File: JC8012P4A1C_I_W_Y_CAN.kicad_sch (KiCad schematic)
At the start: 31 parts, among them J1 610110249121, J2 68711414522, J3 653104131822, Q1 DMP6050SSD, U1 TLE9250VSJ, U2 171030601

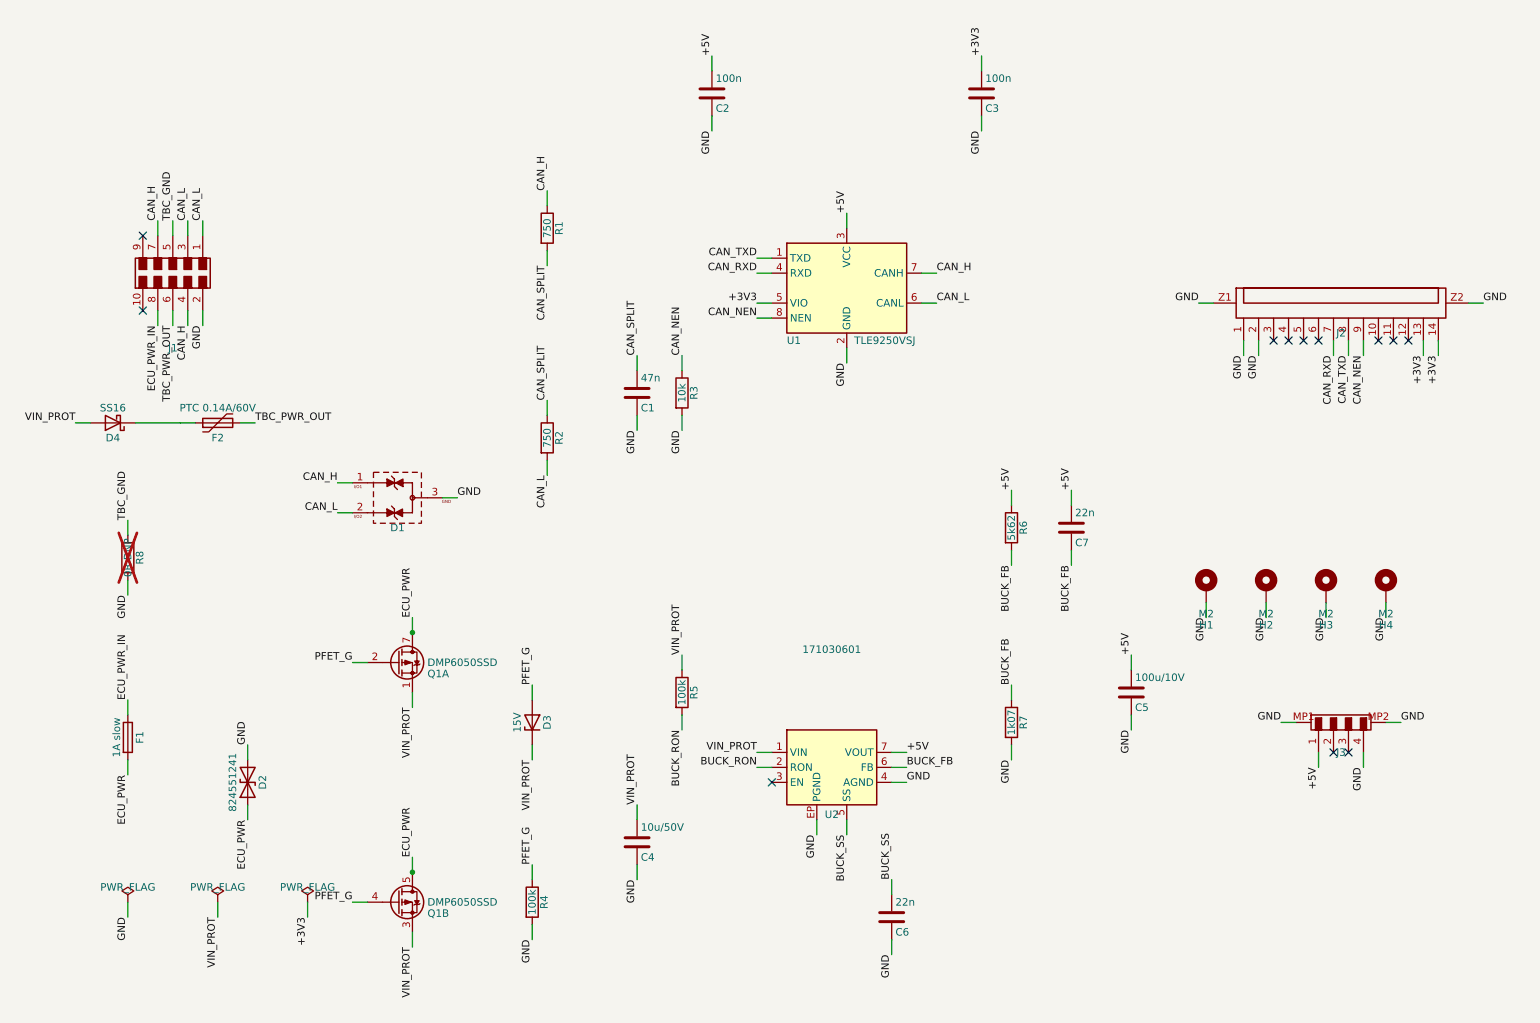
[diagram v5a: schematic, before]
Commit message: Power supply on its own sheet, EMI filter, UVLO, part numbers
Schematic:
- New hierarchical sheet "Versorgung" (power.kicad_sch) with input
  protection, EMI filter, buck converter and TBC supply; connected to
  the main sheet by global labels ECU_PWR_IN, TBC_PWR_OUT, +5V, GND.
  Netlist checked: same parts and connections as before the split.
- Input EMI filter as recommended in the 171030601 datasheet (p. 47,
  EN55022 class B): C8 1 uF (885012209047) + L2 10 uH WE-PD2 (74477410)
- C9 47 uF/50 V SMD electrolytic (865080649013, D8 x 6.5 mm) damping
  the input, behind the reverse polarity protection
- Second input MLCC C12 10 uF/50 V X7R (datasheet: >= 10 uF after
  derating), output C5/C11 2 x 47 uF/10 V X5R + C10 220 uF polymer
  (875105244013), as on the Wuerth evaluation board
- UVLO divider R9 57k6 / R10 10k: on at ~8.0 V, off at ~7.4 V,
  EN stays below 6.5 V up to the 38.9 V TVS clamp voltage
- Wuerth part numbers (MPN, manufacturer, datasheet) on all
  capacitors and L2. Several Wuerth KiCad library symbols carry a
  wrong Value/Footprint (shifted to the neighbour part); the values
  and footprints were taken from the datasheets instead.

Board:
- Footprints of the new parts imported (not placed yet), orphaned
  footprints from before the sheet split removed

Co-Authored-By: Claude Opus 5.5 <noreply@anthropic.com>
Claude-Session: https://claude.ai/code/session_014h8cGi8SRWthYdGFH1Qgzz
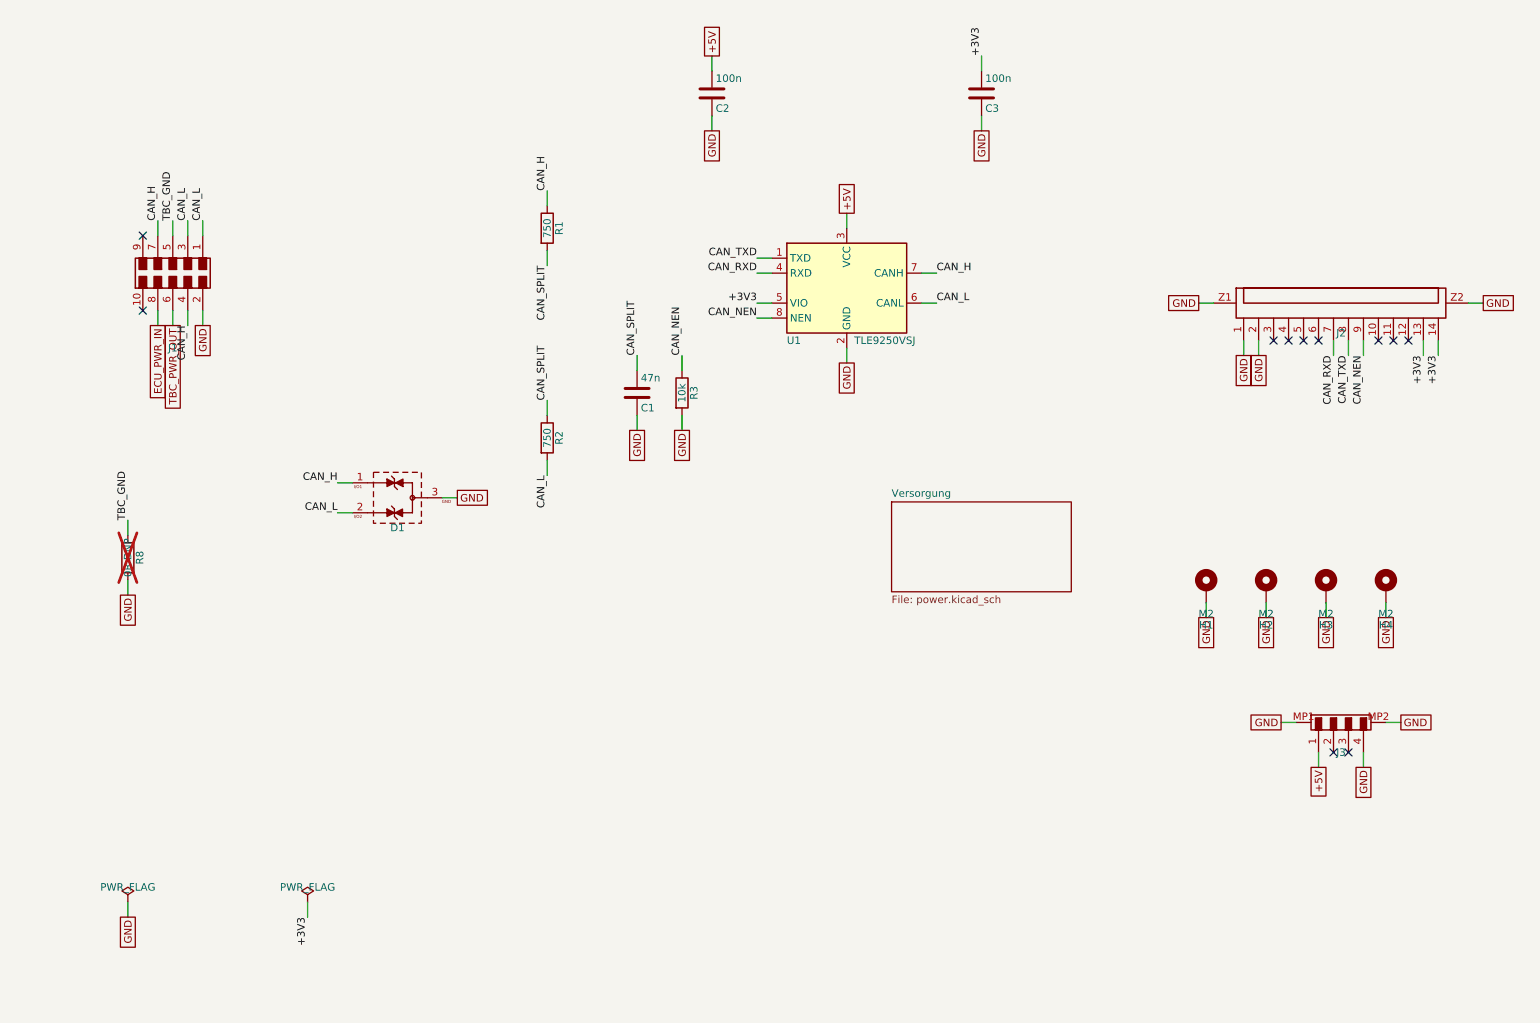
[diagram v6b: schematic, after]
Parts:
- removed C4: 10u/50V, Capacitor_SMD:C_1210_3225Metric, symbol Device:C
- removed C5: 100u/10V, Capacitor_SMD:C_1210_3225Metric, symbol Device:C
- removed C6, C7: 22n, Capacitor_SMD:C_0603_1608Metric, symbol Device:C
- removed D2: 824551241, JC8012P4A1C_CAN:D_Wurth_WE-TVSP-DO214-AB-3000W_BI, symbol Device:D_TVS
- removed D3: 15V, Diode_SMD:D_SOD-123, symbol Device:D_Zener
- removed D4: SS16, Diode_SMD:D_SMA, symbol Device:D_Schottky
- removed F1: 1A slow, Fuse:Fuse_1206_3216Metric, symbol Device:Fuse
- removed F2: PTC 0.14A/60V, Fuse:Fuse_1812_4532Metric, symbol Device:Polyfuse
- removed Q1: DMP6050SSD, Package_SO:SOIC-8_3.9x4.9mm_P1.27mm, symbol Transistor_FET:DMP6050SSD
- removed R4, R5: 100k, Resistor_SMD:R_0603_1608Metric, symbol Device:R
- removed R6: 5k62, Resistor_SMD:R_0603_1608Metric, symbol Device:R
- removed R7: 1k07, Resistor_SMD:R_0603_1608Metric, symbol Device:R
- removed U2: 171030601, JC8012P4A1C_CAN:U_Wurth_WPME-VDRM-TO263-7EP, symbol JC8012P4A1C_CAN:171030601
- C1: MPN (none) -> 885012206093; Manufacturer (none) -> Wurth Elektronik
- C2, C3: MPN (none) -> 885012206095; Manufacturer (none) -> Wurth Elektronik
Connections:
- no-connect marks 12 -> 11
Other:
- added sheet Versorgung (power.kicad_sch)

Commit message: MPN and manufacturer fields for all Wuerth parts
D1, D2, J1, J2, J3, U2: added MPN and Manufacturer; D2 also got its
datasheet link (generic D_TVS symbol). All 19 Wuerth parts now carry
MPN, manufacturer and datasheet link for the BOM.

Co-Authored-By: Claude Opus 5.5 <noreply@anthropic.com>
Claude-Session: https://claude.ai/code/session_014h8cGi8SRWthYdGFH1Qgzz
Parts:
- D1: MPN (none) -> 824094024; Manufacturer (none) -> Wurth Elektronik
- J1: MPN (none) -> 610110249121; Manufacturer (none) -> Wurth Elektronik
- J2: MPN (none) -> 68711414522; Manufacturer (none) -> Wurth Elektronik
- J3: MPN (none) -> 653104131822; Manufacturer (none) -> Wurth Elektronik
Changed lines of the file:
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@@
 			)
 		)
+    (property "MPN" "824094024" (at 76.2 114.3 0)
+      (effects (font (size 1.27 1.27)) (hide yes))
+    )
+    (property "Manufacturer" "Wurth Elektronik" (at 76.2 114.3 0)
+      (effects (font (size 1.27 1.27)) (hide yes))
+    )
 		(pin "1"
 		)
@@
 			)
 		)
+    (property "MPN" "653104131822" (at 236.22 152.4 0)
+      (effects (font (size 1.27 1.27)) (hide yes))
+    )
+    (property "Manufacturer" "Wurth Elektronik" (at 236.22 152.4 0)
+      (effects (font (size 1.27 1.27)) (hide yes))
+    )
 		(pin "1"
 		)
@@
 			)
 		)
+    (property "MPN" "68711414522" (at 236.22 81.28 0)
+      (effects (font (size 1.27 1.27)) (hide yes))
+    )
+    (property "Manufacturer" "Wurth Elektronik" (at 236.22 81.28 0)
+      (effects (font (size 1.27 1.27)) (hide yes))
+    )
 		(pin "1"
 		)
@@
 			)
 		)
-		(pin "1"
-		)
+    (property "MPN" "610110249121" (at 38.1 76.2 0)
+      (effects (font (size 1.27 1.27)) (hide yes))
+    )
+    (property "Manufacturer" "Wurth Elektronik" (at 38.1 76.2 0)
+      (effects (font (size 1.27 1.27)) (hide yes))
+    )
+		(pin "1"
+		)

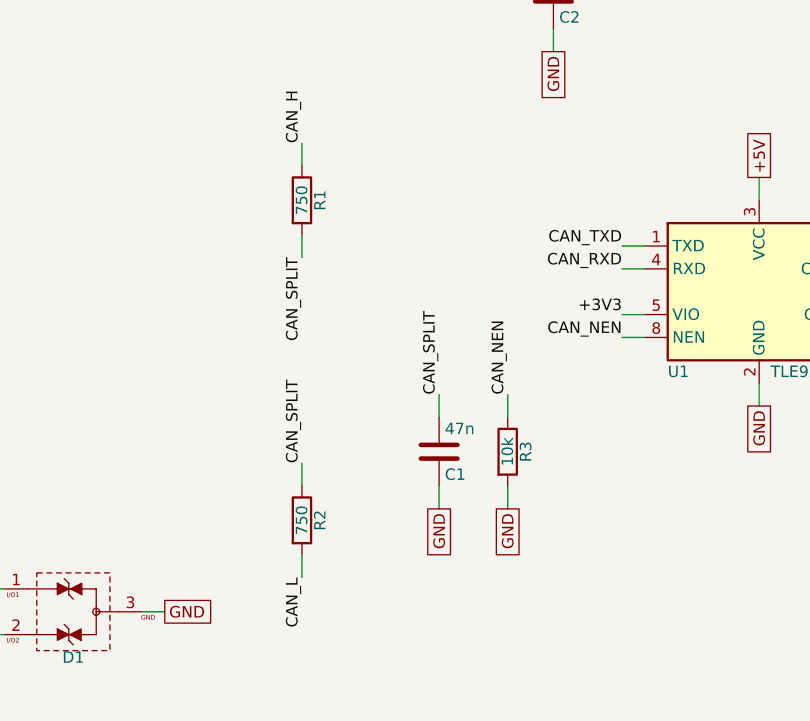
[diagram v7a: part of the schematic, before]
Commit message: Part numbers for all remaining parts, Q1 -> Si4948BEY
- Resistors Yageo RC series 1 %. R1/R2 (split termination 750R) in
  1206 / 0.25 W: ISO 11783-2 asks for >= 125 mW for the termination
  resistors; worst case (CAN_H shorted to 24 V) is ~0.19 W each.
- D3 onsemi MMSZ5245BT1G (15 V), D4 Diodes B160-13-F (60 V Schottky)
- F1 Littelfuse 0452001.MRL NANO2 Slo-Blo 1 A / 125 V (1206 slow fuses
  are only rated 32-63 V), footprint changed to NANO2
- F2 Bourns MF-MSMF014-2 (PTC 0.14 A / 60 V, 1812)
- Q1 Vishay SI4948BEY-T1-E3 instead of the unavailable DMP6050SSD:
  dual P-ch 60 V, same SO-8 pinout (S1 G1 S2 G2 D2 D2 D1 D1), both
  halves in parallel (~60 mOhm)
- U1 Infineon TLE9250VSJXUMA1
- Every part now has MPN and manufacturer fields
- Board updated with F8 (new footprints for R1/R2/F1)

Part numbers derived from the manufacturers' naming schemes; check
availability with the Mouser BOM import before ordering.

Co-Authored-By: Claude Opus 5.5 <noreply@anthropic.com>
Claude-Session: https://claude.ai/code/session_014h8cGi8SRWthYdGFH1Qgzz
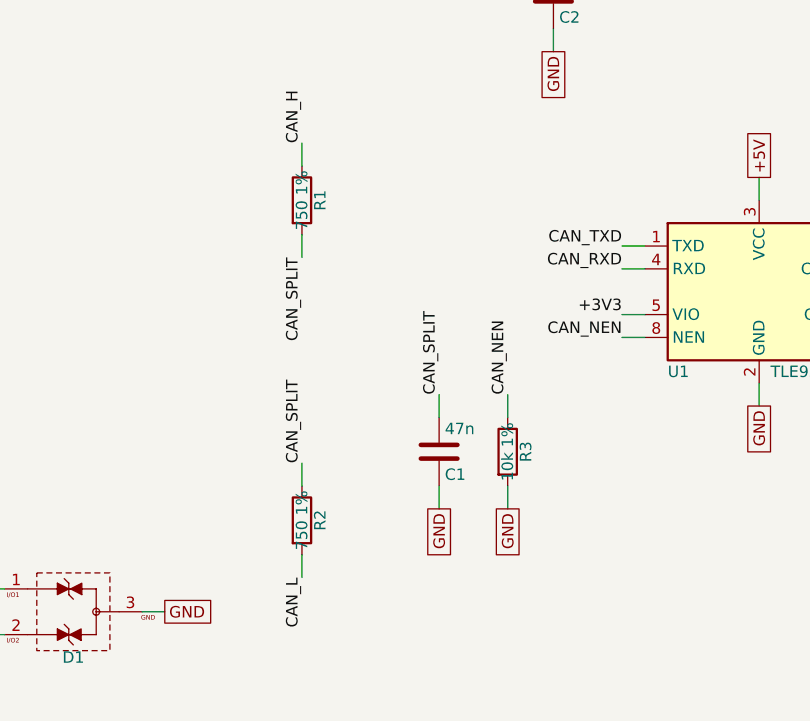
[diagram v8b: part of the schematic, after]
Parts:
- R1, R2: value 750 -> 750 1%; footprint Resistor_SMD:R_0603_1608Metric -> Resistor_SMD:R_1206_3216Metric; MPN (none) -> RC1206FR-07750RL; Manufacturer (none) -> Yageo
- R3: value 10k -> 10k 1%; MPN (none) -> RC0603FR-0710KL; Manufacturer (none) -> Yageo
- R8: MPN (none) -> RC0603JR-070RL; Manufacturer (none) -> Yageo
- U1: MPN (none) -> TLE9250VSJXUMA1; Manufacturer (none) -> Infineon
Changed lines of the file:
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@@
 			)
 		)
-		(property "Value" "750"
+		(property "Value" "750 1%"
 			(at 101.6 104.14 90)
 			(show_name no)
@@
 			)
 		)
-		(property "Footprint" "Resistor_SMD:R_0603_1608Metric"
+		(property "Footprint" "Resistor_SMD:R_1206_3216Metric"
 			(at 99.822 104.14 90)
 			(hide yes)
@@
 					(size 1.27 1.27)
 				)
+			)
+		)
+		(property "Manufacturer" "Yageo"
+			(at 101.6 104.14 0)
+			(effects
+				(font
+					(size 1.27 1.27)
+				)
+				(hide yes)
+			)
+		)
+		(property "MPN" "RC1206FR-07750RL"
+			(at 101.6 104.14 0)
+			(effects
+				(font
+					(size 1.27 1.27)
+				)
+				(hide yes)
 			)
 		)
@@
 			)
 		)
-		(property "Value" "750"
+		(property "Value" "750 1%"
 			(at 101.6 68.58 90)
 			(show_name no)
@@
 			)
 		)
-		(property "Footprint" "Resistor_SMD:R_0603_1608Metric"
+		(property "Footprint" "Resistor_SMD:R_1206_3216Metric"
 			(at 99.822 68.58 90)
 			(hide yes)
@@
 					(size 1.27 1.27)
 				)
+			)
+		)
+		(property "Manufacturer" "Yageo"
+			(at 101.6 68.58 0)
+			(effects
+				(font
+					(size 1.27 1.27)
+				)
+				(hide yes)
+			)
+		)
+		(property "MPN" "RC1206FR-07750RL"
+			(at 101.6 68.58 0)
+			(effects
+				(font
+					(size 1.27 1.27)
+				)
+				(hide yes)
 			)
 		)
@@
 			)
 		)
-		(property "Value" "10k"
+		(property "Value" "10k 1%"
 			(at 124.46 96.52 90)
 			(show_name no)
@@
 					(size 1.27 1.27)
 				)
+			)
+		)
+		(property "Manufacturer" "Yageo"
+			(at 124.46 96.52 0)
+			(effects
+				(font
+					(size 1.27 1.27)
+				)
+				(hide yes)
+			)
+		)
+		(property "MPN" "RC0603FR-0710KL"
+			(at 124.46 96.52 0)
+			(effects
+				(font
+					(size 1.27 1.27)
+				)
+				(hide yes)
 			)
 		)
@@
 			)
 		)
+		(property "Manufacturer" "Infineon"
+			(at 152.4 78.74 0)
+			(effects
+				(font
+					(size 1.27 1.27)
+				)
+				(hide yes)
+			)
+		)
+		(property "MPN" "TLE9250VSJXUMA1"
+			(at 152.4 78.74 0)
+			(effects
+				(font
+					(size 1.27 1.27)
+				)
+				(hide yes)
+			)
+		)
 		(property "Description" "Infineon TLE9250VSJ High-Speed CAN Transceiver, separate VIO, NEN (low = normal mode, internal pull-up to VIO), PG-DSO-8 (SOIC-8). Graphics derived from TJA1049T-3, pin 8 renamed STB->NEN."
 			(at 152.4 78.74 0)
@@
 			)
 		)
+		(property "Manufacturer" "Yageo"
+			(at 30.48 124.46 0)
+			(effects
+				(font
+					(size 1.27 1.27)
+				)
+				(hide yes)
+			)
+		)
+		(property "MPN" "RC0603JR-070RL"
+			(at 30.48 124.46 0)
+			(effects
+				(font
+					(size 1.27 1.27)
+				)
+				(hide yes)
+			)
+		)
